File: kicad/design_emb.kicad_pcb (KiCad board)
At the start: 2 copper layers, 103 parts, among them J1 Conn_01x03, J2 Barrel_Jack, J3 USB_A, J4 Conn_01x03, J5 Conn_02x11_Counter_Clockwise, J6 Conn_02x10_Counter_Clockwise, J7 Screw_Terminal_01x02, J8 Screw_Terminal_01x02, U1 SRX.X.TCT, U10 S25FL116KOXNFIQ-11, U2 SRX.X.TCT, U3 STM32F446ZETx, U4 ICE40HX1K, U5 TLV1117LV33DCYR, U6 TLV1117LV33DCYR, U7 TLV1117LV12DCYR, U8 OMEGA2, U9 RCLAMP0502B

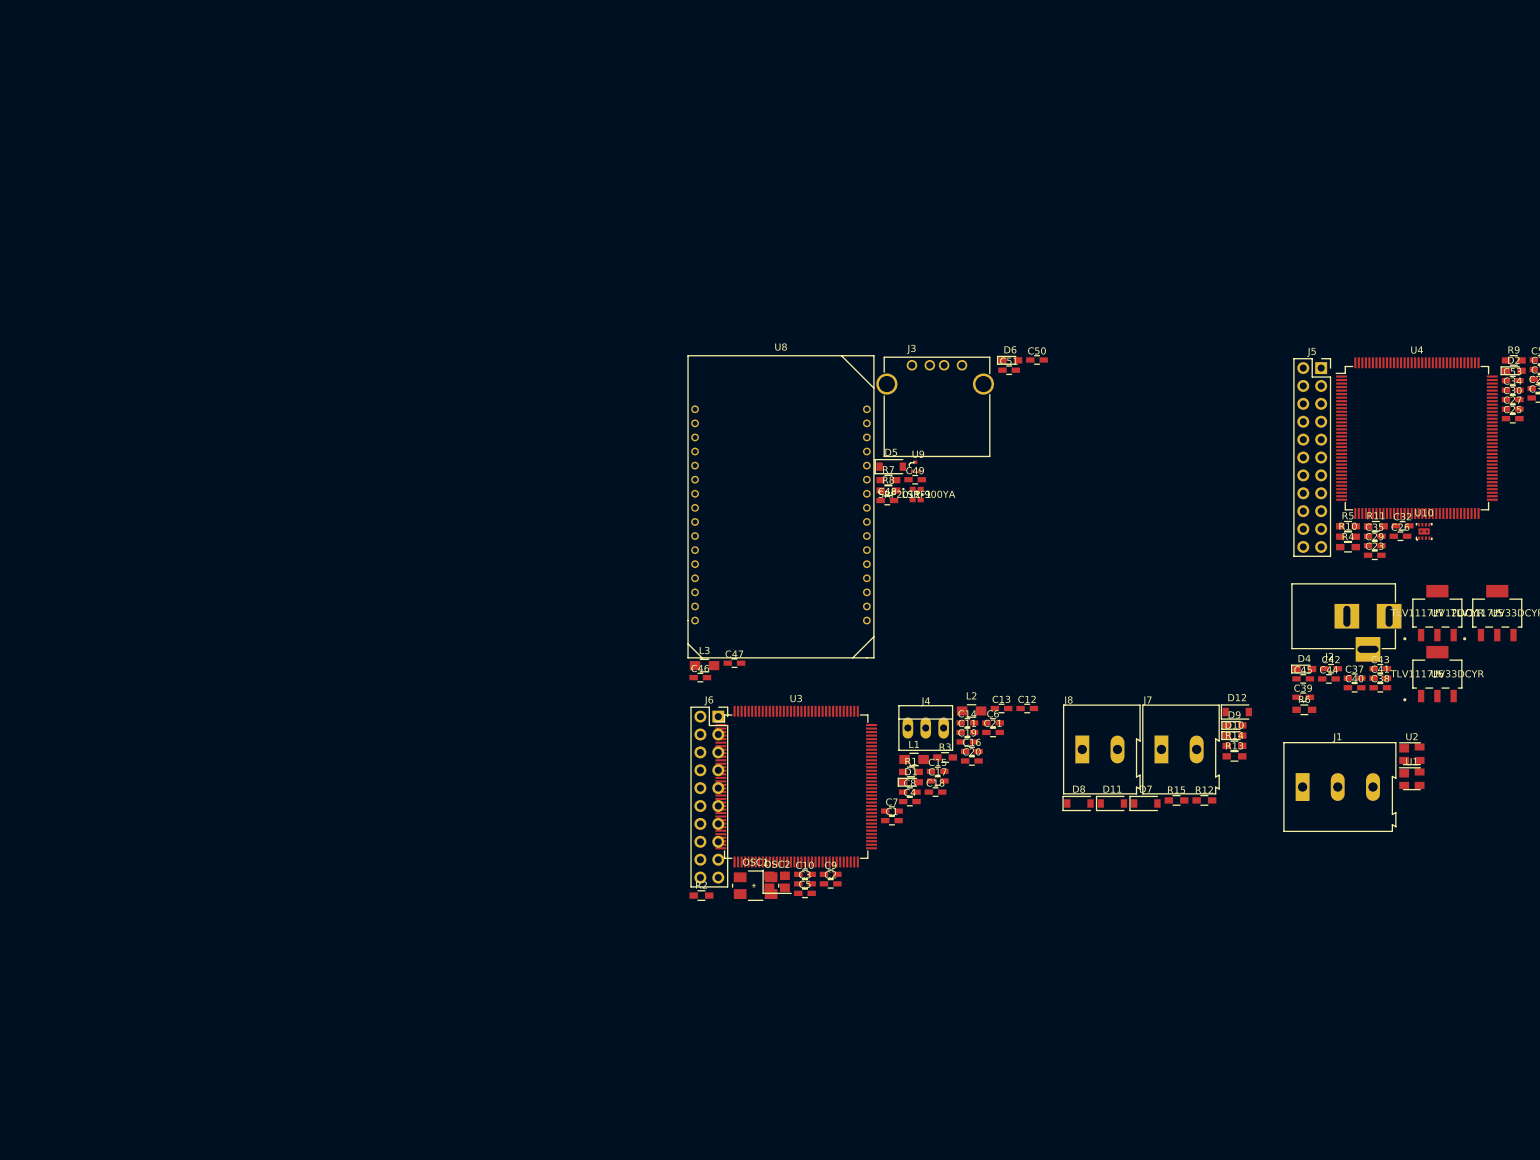
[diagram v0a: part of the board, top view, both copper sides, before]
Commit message: bus SPI, FMC_A Y FMC_NBL
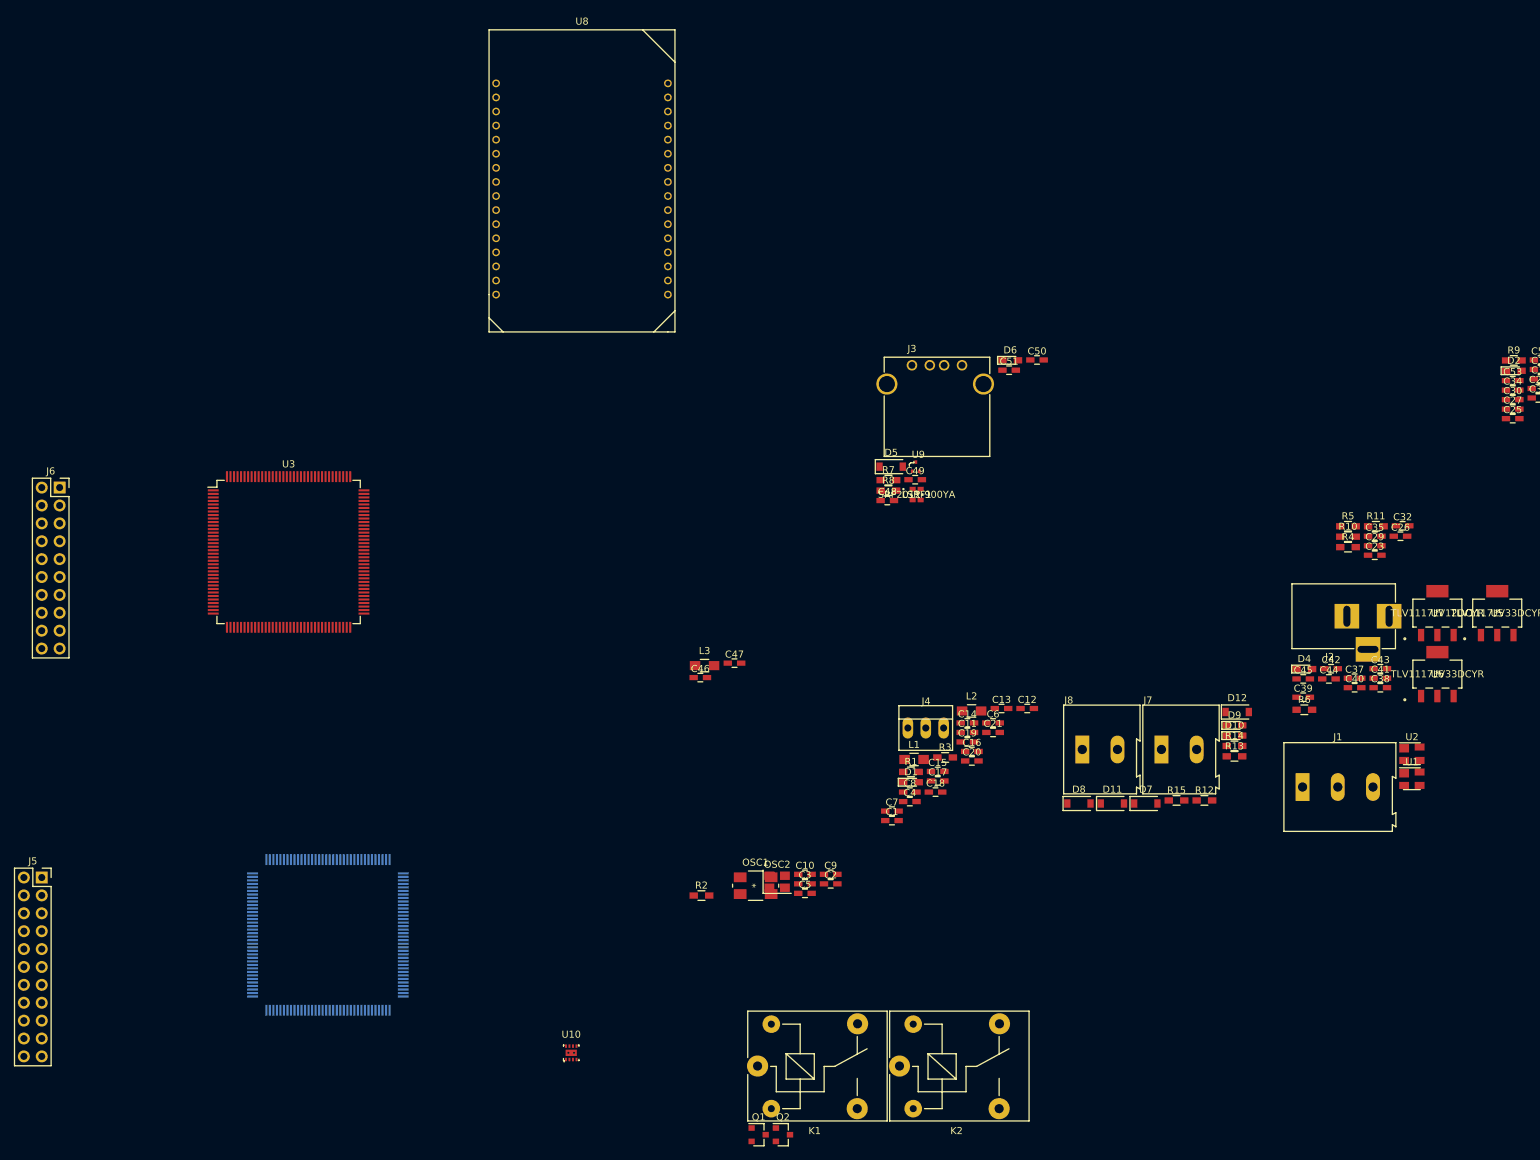
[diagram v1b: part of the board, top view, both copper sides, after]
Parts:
- added K1: SANYOU_SRD_Form_C, Relays_THT:Relay_SPDT_SANYOU_SRD_Series_Form_C, F.Cu at (128.1, 179.7)
- added K2: SANYOU_SRD_Form_C, Relays_THT:Relay_SPDT_SANYOU_SRD_Series_Form_C, F.Cu at (148.2, 179.7)
- added Q1: MMBT3904, TO_SOT_Packages_SMD:SOT-23, F.Cu at (128.2, 189.4)
- added Q2: MMBT3904, TO_SOT_Packages_SMD:SOT-23, F.Cu at (131.7, 189.4)
- R9: value 4.7k -> 10k
- U4: footprint Housings_QFP:LQFP-144_20x20mm_Pitch0.5mm -> ICE40LPH:LQFP-144_20x20mm_Pitch0.5mm
- moved J5 195.6 mm to (26.4, 152.9)
- moved U4 170.0 mm to (67.1, 161.0), turned to 180 degrees
- moved U10 142.0 mm to (101.6, 177.8)
- moved J6 99.0 mm to (29.0, 97.5)
- moved U3 79.4 mm to (61.5, 106.7)
- moved U8 54.2 mm to (90.9, 40.1)
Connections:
- R10 pad 2: /sheet3/SPI3 -> /Sheet2/SPI3
- R11 pad 1: /sheet3/SPI1 -> /Sheet2/SPI1
- R9 pad 1: /sheet3/SPI2 -> /Sheet2/SPI2
- U10 pad 1: /sheet3/SPI0 -> /Sheet2/SPI0
- U10 pad 2: /sheet3/SPI2 -> /Sheet2/SPI2
- U10 pad 5: /sheet3/SPI3 -> /Sheet2/SPI3
- U10 pad 6: /sheet3/SPI1 -> /Sheet2/SPI1
- U3 pad 1: /Sheet1/FMC_A23 -> /Sheet1/FMCA23
- U3 pad 111: Net-(U3-Pad111) -> /Sheet1/UART4_TX
- U3 pad 112: Net-(U3-Pad112) -> /Sheet1/UART4_RX
- U3 pad 113: /Sheet1/UART5_TX -> Net-(U3-Pad113)
- U3 pad 128: /Sheet1/FMC_A24 -> /Sheet1/FMCA24
- U3 pad 143: /Sheet1/VDD_3V3 -> VDD
- U3 pad 2: /Sheet1/FMC_A19 -> /Sheet1/FMCA19
- U3 pad 3: /Sheet1/FMC_A20 -> /Sheet1/FMCA20
- U3 pad 4: /Sheet1/FMC_A21 -> /Sheet1/FMCA21
- U3 pad 5: /Sheet1/FMC_A22 -> /Sheet1/FMCA22
- U4 pad 102: /sheet3/FMCA22 -> /Sheet1/FMCA22
- U4 pad 104: /sheet3/FMCA21 -> /Sheet1/FMCA21
- U4 pad 105: /sheet3/FMCA20 -> /Sheet1/FMCA20
- U4 pad 106: /sheet3/FMCA19 -> /Sheet1/FMCA19
- U4 pad 107: /sheet3/FMCA23 -> /Sheet1/FMCA23
- U4 pad 112: /sheet3/FMCNBL0 -> /Sheet1/FMCNBL0
- U4 pad 113: /sheet3/FMCNBL1 -> /Sheet1/FMCNBL1
- U4 pad 122: /sheet3/FMCA24 -> /Sheet1/FMCA24
- U4 pad 25: /sheet3/FMCA18 -> /Sheet1/FMCA18
- U4 pad 26: /sheet3/FMCA17 -> /Sheet1/FMCA17
- U4 pad 28: /sheet3/FMCA16 -> /Sheet1/FMCA16
- U4 pad 67: /sheet3/SPI3 -> /Sheet2/SPI3
- U4 pad 68: /sheet3/SPI2 -> /Sheet2/SPI2
- U4 pad 70: /sheet3/SPI1 -> /Sheet2/SPI1
- U4 pad 71: /sheet3/SPI0 -> /Sheet2/SPI0
- U8 pad 8: /Sheet1/UART5_TX -> /Sheet1/UART4_TX
- U8 pad 9: /Sheet2/UART_TX -> /Sheet1/UART4_RX

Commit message: design_emb.ses
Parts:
- added R16: 100, Resistors_SMD:R_0603_HandSoldering, F.Cu at (108.7, 117.6)
- added R17: 100, Resistors_SMD:R_0603_HandSoldering, F.Cu at (108.7, 119.1)
- added R18: 100, Resistors_SMD:R_0603_HandSoldering, F.Cu at (112.6, 117.6)
- R11: value 10k -> 4.7k
- R9: value 10k -> 100
- moved C25 126.8 mm to (109.6, 104.1)
- moved C27 126.8 mm to (109.6, 102.8)
- moved C30 126.8 mm to (109.6, 101.4)
- moved C34 126.8 mm to (109.6, 100.1)
- moved C53 126.8 mm to (109.6, 98.7)
- moved D2 126.8 mm to (109.8, 97.3)
- moved R9 126.8 mm to (109.8, 95.9)
- moved C22 126.8 mm to (113.2, 99.8)
- moved C24 126.8 mm to (117.2, 97.2)
- moved C28 126.8 mm to (117.2, 95.8)
- moved C31 126.8 mm to (113.5, 98.5)
- moved C33 126.8 mm to (113.5, 97.2)
- moved C36 126.8 mm to (113.2, 101.2)
- moved C52 126.8 mm to (113.5, 95.8)
- moved J4 92.1 mm to (59.7, 152.4)
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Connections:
- R10 pad 2: /Sheet2/SPI3 -> /sheet3/SPI0
- R11 pad 1: /Sheet2/SPI1 -> /sheet3/SPI1
- R12 pad 1: Net-(Q1-Pad1) -> Net-(R12-Pad1)
- R13 pad 1: Net-(Q2-Pad1) -> Net-(R13-Pad1)
- R9 pad 1: /Sheet2/SPI2 -> Net-(R9-Pad1)
- R9 pad 2: /Sheet4/+3V3_FPGA -> /Sheet2/SPI0
- U10 pad 1: /Sheet2/SPI0 -> /sheet3/SPI0
- U10 pad 2: /Sheet2/SPI2 -> /sheet3/SPI2
- U10 pad 5: /Sheet2/SPI3 -> /sheet3/SPI3
- U10 pad 6: /Sheet2/SPI1 -> /sheet3/SPI1
- U4 pad 112: /Sheet1/FMCNBL0 -> /sheet3/FMCNBL0
- U4 pad 113: /Sheet1/FMCNBL1 -> /sheet3/FMCNBL1
- U4 pad 67: /Sheet2/SPI3 -> /sheet3/SPI3
- U4 pad 68: /Sheet2/SPI2 -> /sheet3/SPI2
- U4 pad 70: /Sheet2/SPI1 -> /sheet3/SPI1
- U4 pad 71: /Sheet2/SPI0 -> /sheet3/SPI0
- U8 pad 10: /Sheet2/SPI3 -> Net-(R18-Pad1)
- U8 pad 11: /Sheet2/SPI2 -> Net-(R17-Pad1)
- U8 pad 12: /Sheet2/SPI1 -> Net-(R16-Pad1)
- U8 pad 13: /Sheet2/SPI0 -> Net-(R9-Pad1)
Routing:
- net GND: track 0.00 -> 285.0 mm
- net VDD: track 0.00 -> 195.6 mm
- net /Sheet4/+3V3_FPGA: track 0.00 -> 93.4 mm, vias 0 -> 1
- net +5VA: track 0.00 -> 93.3 mm, vias 0 -> 1
- net Net-(J3-Pad5): track 0.00 -> 91.7 mm
- net /sheet3/GPIO3: track 0.00 -> 84.0 mm
- net /sheet3/GPIO4: track 0.00 -> 82.9 mm
- net Net-(D12-Pad2): track 0.00 -> 81.8 mm, vias 0 -> 1
- net /Sheet1/USR9: track 0.00 -> 69.3 mm, vias 0 -> 2
- net /Sheet4/+1V2_FPGA: track 0.00 -> 69.2 mm, vias 0 -> 1
- net /Sheet1/USR8: track 0.00 -> 66.1 mm, vias 0 -> 1
- net /Sheet1/USR3: track 0.00 -> 65.4 mm, vias 0 -> 1
- net /Sheet1/USR14: track 0.00 -> 65.1 mm, vias 0 -> 1
- net /Sheet1/USR10: track 0.00 -> 64.2 mm, vias 0 -> 1
- net /Sheet1/USR4: track 0.00 -> 63.0 mm, vias 0 -> 1
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
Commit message: design_emb.kicad_pcb
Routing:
- net /SERIAL_RX: track 0.00 -> 112.5 mm, vias 0 -> 1
- net /SERIAL_TX: track 0.00 -> 106.4 mm, vias 0 -> 1
- net GND: track 285.0 -> 367.4 mm
- net Net-(J3-Pad5): track 91.7 -> 17.8 mm
- net Net-(J8-Pad1): track 0.00 -> 70.5 mm
- net /Sheet1/USR5: track 0.00 -> 69.1 mm, vias 0 -> 1
- net /Sheet1/USR7: track 0.00 -> 68.0 mm, vias 0 -> 1
- net /Sheet1/USR12: track 0.00 -> 66.2 mm, vias 0 -> 1
- net /Sheet1/USR1: track 0.00 -> 65.5 mm, vias 0 -> 1
- net /Sheet1/OSC_IN: track 0.00 -> 63.5 mm
- net /sheet3/GPIO16: track 56.0 -> 0.00 mm, vias 1 -> 0
- net /Sheet1/OSC32_OUT: track 0.00 -> 55.1 mm
- net /sheet3/GPIO18: track 55.1 -> 0.00 mm, vias 1 -> 0
- net /sheet3/GPIO14: track 54.9 -> 0.00 mm, vias 1 -> 0
- net /sheet3/GPIO19: track 52.2 -> 0.00 mm, vias 1 -> 0
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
